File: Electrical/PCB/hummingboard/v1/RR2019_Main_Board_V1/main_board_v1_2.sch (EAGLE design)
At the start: 129 parts, among them CN1 MIRCO_B, J1 JTAG_SWD, J10 I2C_5V_4, J11 SERVO_LEFT, J12 SERVO_RIGHT, J13 ESC, J14 5V_INPUT, J15 QUAD_ENCODER_2, J17 I2C_5V_FXIO_1, J18 I2C_5V_FXIO_2, J2 REAR_ENCODER, J20 QUAD_ENCODER_1, J21 BLDC_HALL, J22 SPI_FXIO_1, J3 FRONT_ENCODER, J4 I2C_3V3_1, J5 SPI_2, J6 WIRELESS_MODULE, J7 UART_0, J8 UART_2, J9 STEERING_ANGLE, Q1 BSS138, Q2 BSS138, Q3 PMOS_SOT23, Q4 BSS138, Q5 BSS138, Q6 BSS138, Q7 BSS138, U1 MPU-9250(IMU)

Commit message: update on layout
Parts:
- added C23: TBD, RobotRacing2019_Master:CAP0603
- added J16: 7.2V_INPUT, RobotRacing2019_Master:PINHEAD-2-VERTICAL
- added L3: TBD, RobotRacing2019_Master:IND0603
- added R42: TBD, RobotRacing2019_Master:RES0603
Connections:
- removed net PTA11: U$50.1
- new net +7.2V: C23.1, J11.1, J12.1, L3.2
- new net N$34: J16.1, R42.2
- new net N$36: L3.1, R42.1
- net +5V: no longer J11.1, J12.1
- net GND: now also C23.2, J16.2
- net PTA11_/_FTM1_CH5: now also U$50.1
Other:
- moved on the sheet: J11, J12, J13

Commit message: [Journey Begins From Here] + new simulations and PCBs
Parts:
- removed J1: JTAG_SWD, RobotRacing2019_Master:10-PIN_SWD
- removed JP12: POWER_2, adafruit:PINHD-1X8BIG
- added C24: 0.1u, RobotRacing2019_Master:CAP0603
- added IC1: OR_SC70-5, RobotRacing2019_Master:OR_SC70-5
- added J19: JETSON_TRIGGER, RobotRacing2019_Master:PINHEAD-2-VERTICAL
- added Q8: BSS138, RobotRacing2019_Master:NMOS_SOT23
- added R43, R44: 10k, RobotRacing2019_Master:RES0603
- added U$44: TEAM_LOGO, RobotRacing2019_Master:TEAM_LOGO
- Q3: value PMOS_SOT23 -> DMP2066LSN
- U$12: value TEAM_LOGO -> SWD_1.27MM; device RobotRacing2019_Master:TEAM_LOGO -> RobotRacing2019_Master:SWD_1.27MM
- renumbered POWER_OFF/ON to OFF/ON
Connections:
- removed net 3V3: JP12.4, JP12.5, JP6.4, JP6.5
- removed net N$16: CN1.ID
- removed net VDD: C1.1, C2.1, C3.1, C4.1, C5.1, C6.1, J15.1, J17.1, J18.1, J20.1, J22.1, J5.1, JP12.1, JP12.2, JP12.3, JP6.1, JP6.2, JP6.3, R10.2, R11.2, R15.2, R18.2, R21.2, R22.2, R24.2, R26.2, R28.2, R29.2, R41.2, R9.2, U$1.VDD, U$1.VDD1, U$1.VDD2, U$1.VDD3, U$1.VDDA, U$1.VREFH
- new net N$35: J19.1, Q8.G
- new net N$38: IC1.A, Q8.D, R44.1
- new net N$39: IC1.OUT, Q3.G, R43.1
- net +3V3: now also JP6.4, JP6.5
- net +VDD: now also C1.1, C2.1, C24.2, C3.1, C4.1, C5.1, C6.1, IC1.VDD, J15.1, J17.1, J18.1, J20.1, J22.1, J5.1, JP6.1, JP6.2, JP6.3, R10.2, R11.2, R15.2, R18.2, R21.2, R22.2, R24.2, R26.2, R28.2, R29.2, R41.2, R43.2, R44.2, R9.2, U$1.VDD, U$1.VDD1, U$1.VDD2, U$1.VDD3, U$1.VDDA, U$1.VREFH, U$12.VCC; no longer J1.VCC
- net GND: now also C24.1, IC1.GND, Q8.S, U$12.GND, U$12.GND2, U$12.GND_DCT, U$12.KEY; no longer J1.GND, J1.GND2, J1.GND_DCT, J1.KEY, JP12.6, JP12.7, JP12.8
- net JTAG_TCLK/SWD_CLK: now also U$12.SWDCLK/TCK; no longer J1.SWDCLK/TCK
- net JTAG_TDI: now also U$12.NC/TDI; no longer J1.NC/TDI
- net JTAG_TDO/SWO: now also U$12.SWO/TDO; no longer J1.SWO/TDO
- net JTAG_TMS/SWD_DIO: now also U$12.SWDIO/TMS; no longer J1.SWDIO/TMS
- net JTAG_TRST_B: now also U$12./R/E/S/E/T; no longer J1./R/E/S/E/T
- net POWER_SHUT_DOWN: now also IC1.B; no longer Q3.G
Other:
- note added: "separe the 7.2V GND"
- note removed: "nominally LOW, turn high when overcurrent is measured - pick low Rds on - handle up to 300mA ?"
- moved on the sheet: C16, JP6

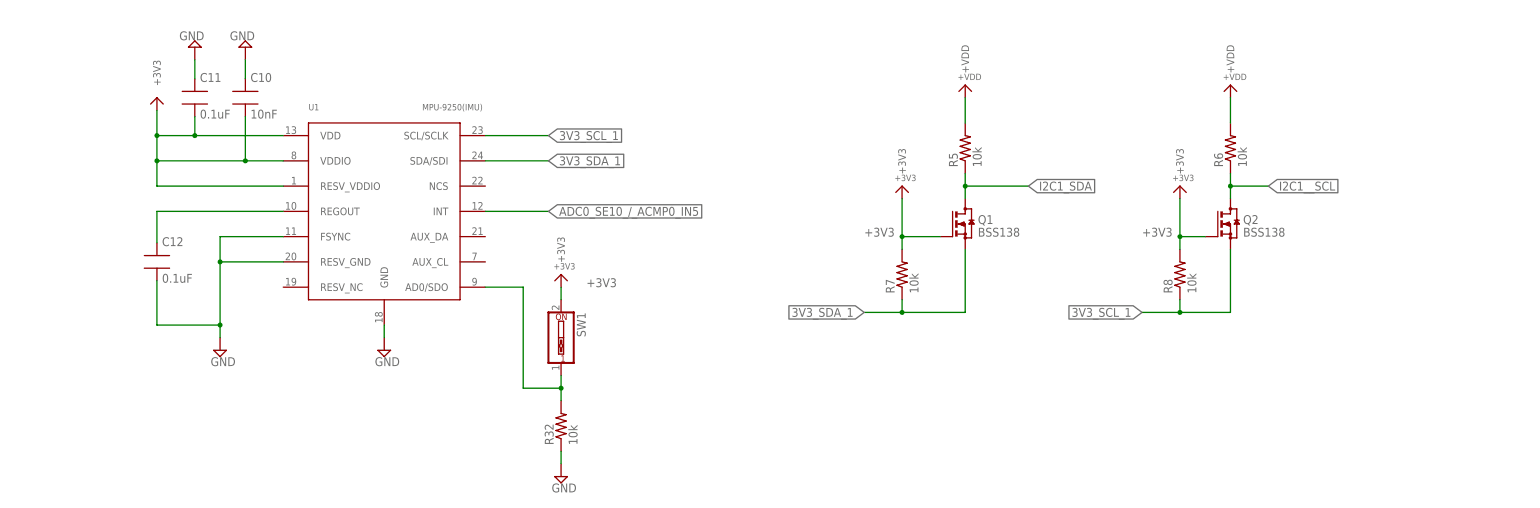
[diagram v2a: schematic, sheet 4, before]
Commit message: add 1.8V LDO and IMU change to ICM-20948
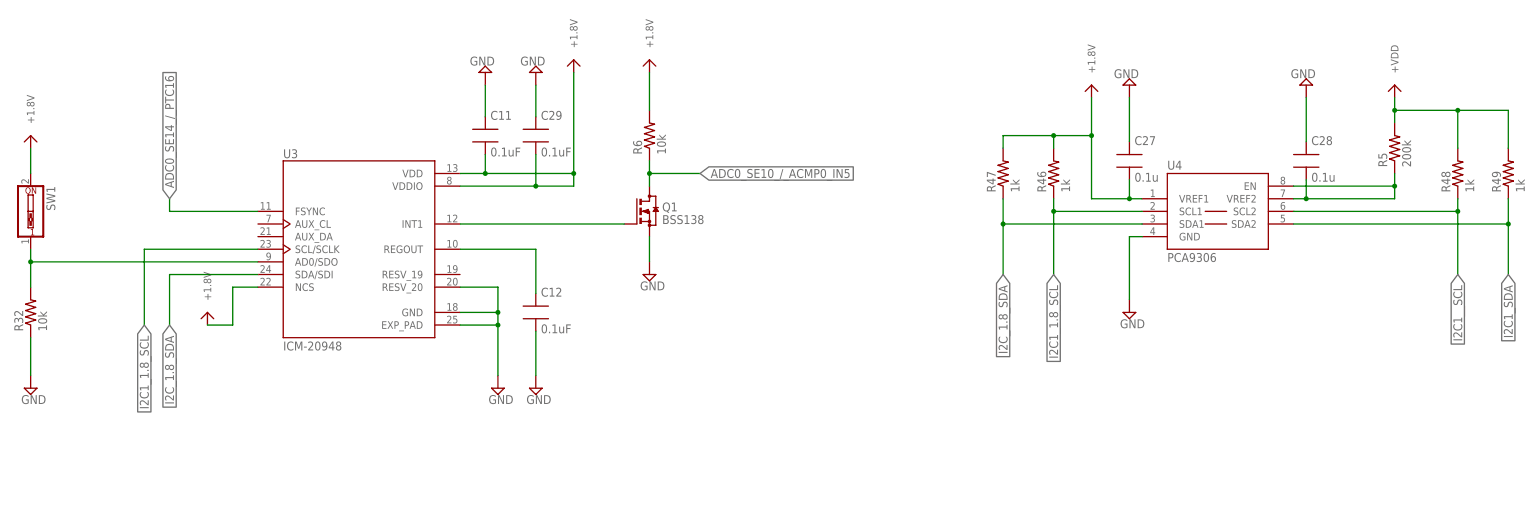
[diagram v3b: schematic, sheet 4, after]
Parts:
- removed C10: 10nF, RobotRacing2019_Master:CAP0603
- removed Q2: BSS138, RobotRacing2019_Master:NMOS_SOT23
- removed R7, R8: 10k, RobotRacing2019_Master:RES0603
- removed U1: MPU-9250(IMU), RobotRacing2019_Master:MPU-9250(IMU)
- added C25, C26: 1uF, RobotRacing2019_Master:CAP0603
- added C27, C28: 0.1u, RobotRacing2019_Master:CAP0603
- added C29: 0.1uF, RobotRacing2019_Master:CAP0603
- added D9: LED_GREEN, RobotRacing2019_Master:LED0603
- added R45: 150, RobotRacing2019_Master:RES0603
- added R46, R47, R48, R49: 1k, RobotRacing2019_Master:RES0603
- added U3: ICM-20948, RobotRacing2019_Master:ICM-20948
- added U4: PCA9306, RobotRacing2019_Master:PCA9306
- added VR2: ADP121-AUJZ18, RobotRacing2019_Master:ADP121
- D3, D4: value LED0603 -> LED_GREEN
- R3, R4: value (none) -> 150
- R5: value 10k -> 200k
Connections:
- new net +1.8V: C11.2, C26.1, C27.2, C29.2, R45.2, R46.2, R47.2, R6.2, SW1.2, U3.NCS, U3.VDD, U3.VDDIO, U4.VREF1, VR2.VOUT
- new net I2C1_1.8_SCL: R46.1, U3.SCL/SCLK, U4.SCL1
- new net I2C_1.8_SDA: R47.1, U3.SDA/SDI, U4.SDA1
- new net N$16: C28.2, R5.1, U4.EN, U4.VREF2
- new net N$37: Q1.G, U3.INT1
- new net N$42: D9.A, R45.1
- net +3V3: no longer C10.2, C11.2, Q1.G, Q2.G, R7.2, R8.2, SW1.2, U1.RESV_VDDIO, U1.VDD, U1.VDDIO
- net +VDD: now also C25.1, R48.2, R49.2, VR2.EN, VR2.VIN; no longer R6.2
- net 3V3_SCL_1: no longer Q2.S, R8.1, U1.SCL/SCLK
- net 3V3_SDA_1: no longer Q1.S, R7.1, U1.SDA/SDI
- net ADC0_SE10_/_ACMP0_IN5: now also Q1.D, R6.1; no longer U1.INT
- net ADC0_SE14_/_PTC16: now also U3.FSYNC
- net GND: now also C25.2, C26.2, C27.1, C28.1, C29.1, D9.C, Q1.S, U3.EXP_PAD, U3.GND, U3.RESV_20, U4.GND, VR2.GND; no longer C10.1, U1.FSYNC, U1.GND, U1.RESV_GND
- net I2C1_SDA: now also R49.1, U4.SDA2; no longer Q1.D, R5.1
- net I2C1__SCL: now also R48.1, U4.SCL2; no longer Q2.D, R6.1
- net N$10: now also U3.REGOUT; no longer U1.REGOUT
- net N$22: now also U3.AD0/SDO; no longer U1.AD0/SDO
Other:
- note added: "5V - 1.8 V LDO"
- note added: "IMU_FSYNC"
- note removed: "* can use AUX_DA / AUX_CL / FSYNC for external sensor via i2c"
- note removed: "pick mosfet with low RDS"
- moved on the sheet: C11, C12, Q1, R32, R5, R6, SW1

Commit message: signal connection complete
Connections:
- removed net 3V3_SCL_1: J4.3
- removed net 3V3_SDA_1: J4.4
- removed net I2C_1.8_SDA: R47.1, U3.SDA/SDI, U4.SDA1
- new net I2C1_1.8_SDA: J4.4, R47.1, U3.SDA/SDI, U4.SDA1
- net +1.8V: now also J4.1
- net +3V3: no longer J4.1
- net I2C1_1.8_SCL: now also J4.3
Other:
- note added: "5V-1V8 level shifter on page4"
- note added: "ICM-20948 in I2C config"
- note removed: "5V-3V3 level shifter on page4"
- note removed: "MPU9250 in I2C config"
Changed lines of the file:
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@@
 <part name="U$26" library="RobotRacing2019_Master" deviceset="+VDD" device=""/>
 <part name="U$28" library="RobotRacing2019_Master" deviceset="+VDD" device=""/>
-<part name="U$29" library="RobotRacing2019_Master" deviceset="+3V3" device=""/>
 <part name="U$30" library="RobotRacing2019_Master" deviceset="+VDD" device=""/>
 <part name="U$31" library="RobotRacing2019_Master" deviceset="+VDD" device=""/>
@@
 <part name="U$23" library="RobotRacing2019_Master" deviceset="+1V8" device=""/>
 <part name="U$24" library="RobotRacing2019_Master" deviceset="+1V8" device=""/>
+<part name="U$21" library="RobotRacing2019_Master" deviceset="+1V8" device=""/>
 </parts>
 <sheets>
@@
 <text x="-195.58" y="-15.24" size="1.778" layer="120">if AD0 -&gt; GND, i2c address = 1101000
 if AD0 -&gt; VDD, i2c address = 1101001</text>
-<text x="-99.06" y="20.32" size="2.54" layer="119">MPU9250 in I2C config</text>
-<text x="-132.08" y="-45.72" size="1.778" layer="117">TP / VIA</text>
-<text x="-119.38" y="-45.72" size="1.778" layer="117">TP / VIA</text>
+<text x="-99.06" y="20.32" size="2.54" layer="119">ICM-20948 in I2C config</text>
+<text x="-132.08" y="-53.34" size="1.778" layer="117">TP / VIA</text>
+<text x="-119.38" y="-53.34" size="1.778" layer="117">TP / VIA</text>
 </plain>
 <instances>
@@
 </segment>
 </net>
-<net name="I2C_1.8_SDA" class="0">
-<segment>
-<pinref part="U4" gate="G$1" pin="SDA1"/>
-<wire x1="76.2" y1="0" x2="48.26" y2="0" width="0.1524" layer="91"/>
-<pinref part="R47" gate="G$1" pin="1"/>
-<wire x1="48.26" y1="0" x2="48.26" y2="5.08" width="0.1524" layer="91"/>
-<wire x1="48.26" y1="0" x2="48.26" y2="-10.16" width="0.1524" layer="91"/>
-<junction x="48.26" y="0"/>
-<label x="48.26" y="-10.16" size="1.778" layer="95" rot="R270" xref="yes"/>
-</segment>
-<segment>
-<pinref part="U3" gate="G$1" pin="SDA/SDI"/>
-<wire x1="-101.6" y1="-10.16" x2="-119.38" y2="-10.16" width="0.1524" layer="91"/>
-<wire x1="-119.38" y1="-10.16" x2="-119.38" y2="-20.32" width="0.1524" layer="91"/>
-<label x="-119.38" y="-20.32" size="1.778" layer="95" rot="R270" xref="yes"/>
-</segment>
-</net>
 <net name="N$16" class="0">
 <segment>
@@
 </segment>
 </net>
+<net name="I2C1_1.8_SDA" class="0">
+<segment>
+<pinref part="U3" gate="G$1" pin="SDA/SDI"/>
+<wire x1="-101.6" y1="-10.16" x2="-119.38" y2="-10.16" width="0.1524" layer="91"/>
+<wire x1="-119.38" y1="-10.16" x2="-119.38" y2="-20.32" width="0.1524" layer="91"/>
+<label x="-119.38" y="-20.32" size="1.778" layer="95" rot="R270" xref="yes"/>
+</segment>
+<segment>
+<pinref part="U4" gate="G$1" pin="SDA1"/>
+<wire x1="76.2" y1="0" x2="48.26" y2="0" width="0.1524" layer="91"/>
+<pinref part="R47" gate="G$1" pin="1"/>
+<wire x1="48.26" y1="0" x2="48.26" y2="5.08" width="0.1524" layer="91"/>
+<wire x1="48.26" y1="0" x2="48.26" y2="-10.16" width="0.1524" layer="91"/>
+<junction x="48.26" y="0"/>
+<label x="48.26" y="-10.16" size="1.778" layer="95" rot="R270" xref="yes"/>
+</segment>
+</net>
 </nets>
 </sheet>
@@
 <wire x1="86.36" y1="-205.74" x2="12.7" y2="-205.74" width="0.1524" layer="206"/>
 <text x="-25.4" y="-101.6" size="1.778" layer="120">pull up on the MCU side</text>
-<text x="10.16" y="-101.6" size="1.778" layer="120">5V-3V3 level shifter on page4</text>
+<text x="10.16" y="-101.6" size="1.778" layer="120">5V-1V8 level shifter on page4</text>
 <text x="-20.32" y="91.44" size="1.778" layer="120">pull up and pull down on the MCU side</text>
 <text x="40.64" y="-261.62" size="1.778" layer="120">connect to uart of JETSON</text>
@@
 <attribute name="VALUE" x="-52.324" y="-100.584" size="1.27" layer="96"/>
 </instance>
-<instance part="U$29" gate="G$1" x="48.26" y="-106.68" smashed="yes">
-<attribute name="VALUE" x="44.196" y="-103.124" size="1.27" layer="96"/>
-</instance>
 <instance part="U$30" gate="G$1" x="-48.26" y="-236.22" smashed="yes">
 <attribute name="VALUE" x="-52.324" y="-235.204" size="1.27" layer="96"/>
@@
 <attribute name="VALUE" x="-12.7" y="116.84" size="1.27" layer="96"/>
 </instance>
+<instance part="U$21" gate="G$1" x="48.26" y="-106.68" smashed="yes"/>
 </instances>
 <busses>
@@
 </segment>
 </net>
-<net name="3V3_SCL_1" class="0">
+<net name="I2C1_1.8_SCL" class="0">
 <segment>
 <pinref part="J4" gate="G$1" pin="3"/>
@@
 </segment>
 </net>
-<net name="3V3_SDA_1" class="0">
+<net name="I2C1_1.8_SDA" class="0">
 <segment>
 <pinref part="J4" gate="G$1" pin="4"/>
@@
 <net name="+3V3" class="0">
 <segment>
-<pinref part="J4" gate="G$1" pin="1"/>
-<wire x1="30.48" y1="-111.76" x2="48.26" y2="-111.76" width="0.1524" layer="91"/>
-<wire x1="48.26" y1="-111.76" x2="73.66" y2="-111.76" width="0.1524" layer="91"/>
-<wire x1="48.26" y1="-111.76" x2="48.26" y2="-106.68" width="0.1524" layer="91"/>
-<junction x="48.26" y="-111.76"/>
-<pinref part="U$29" gate="G$1" pin="+3V3"/>
-<label x="38.1" y="-111.76" size="1.778" layer="95"/>
-</segment>
-<segment>
 <pinref part="J6" gate="G$1" pin="1"/>
 <wire x1="-33.02" y1="33.02" x2="-25.4" y2="33.02" width="0.1524" layer="91"/>
@@
 </segment>
 </net>
+<net name="+1.8V" class="0">
+<segment>
+<pinref part="J4" gate="G$1" pin="1"/>
+<wire x1="30.48" y1="-111.76" x2="48.26" y2="-111.76" width="0.1524" layer="91"/>
+<wire x1="48.26" y1="-111.76" x2="73.66" y2="-111.76" width="0.1524" layer="91"/>
+<wire x1="48.26" y1="-111.76" x2="48.26" y2="-106.68" width="0.1524" layer="91"/>
+<junction x="48.26" y="-111.76"/>
+<pinref part="U$21" gate="G$1" pin="+1.8V"/>
+</segment>
+</net>

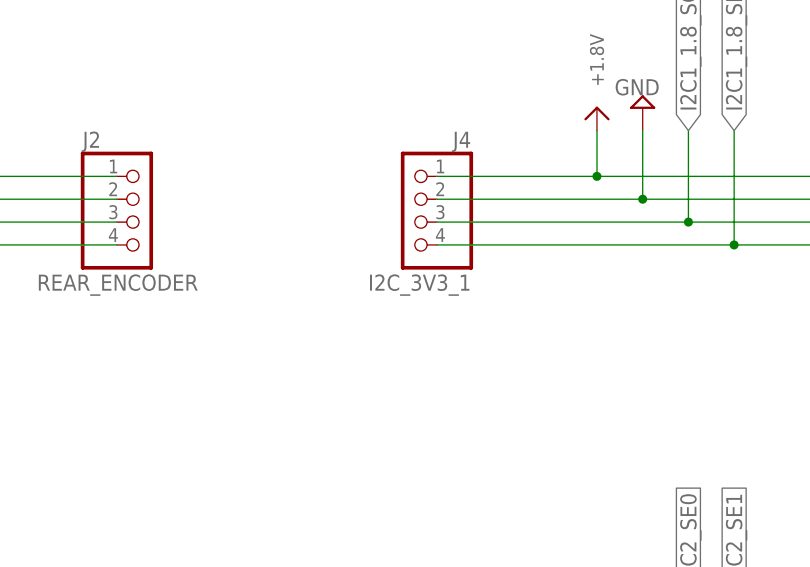
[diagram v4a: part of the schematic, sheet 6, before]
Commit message: add 1V8, 3V3, VUSB power plane
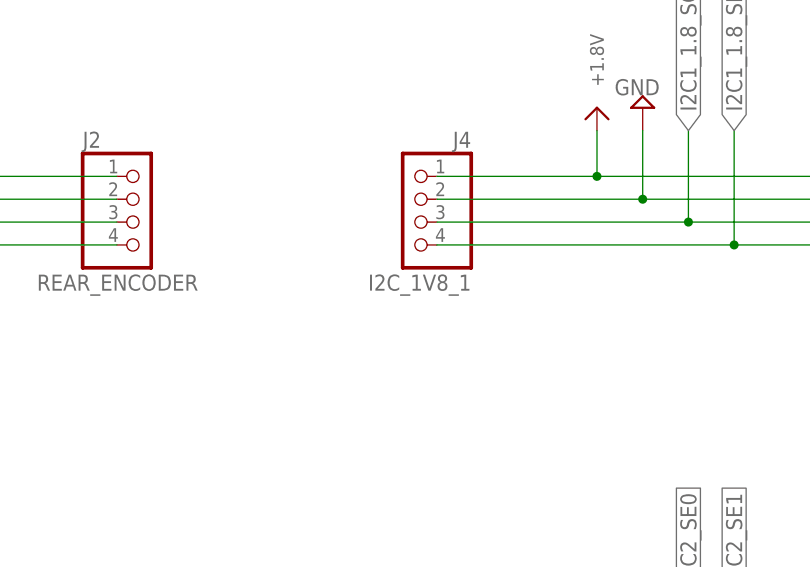
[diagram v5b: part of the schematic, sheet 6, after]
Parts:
- J4: value I2C_3V3_1 -> I2C_1V8_1
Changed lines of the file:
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@@
 <part name="J2" library="RobotRacing2019_Master" deviceset="PINHEAD-4-VERTICAL" device="" value="REAR_ENCODER"/>
 <part name="J3" library="RobotRacing2019_Master" deviceset="PINHEAD-4-VERTICAL" device="" value="FRONT_ENCODER"/>
-<part name="J4" library="RobotRacing2019_Master" deviceset="PINHEAD-4-VERTICAL" device="" value="I2C_3V3_1"/>
+<part name="J4" library="RobotRacing2019_Master" deviceset="PINHEAD-4-VERTICAL" device="" value="I2C_1V8_1"/>
 <part name="J5" library="RobotRacing2019_Master" deviceset="PINHEAD-6-VERTICAL" device="" value="SPI_2"/>
 <part name="J6" library="RobotRacing2019_Master" deviceset="PINHEAD-6-VERTICAL" device="" value="WIRELESS_MODULE"/>

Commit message: add silkscreen for pin info
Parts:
- JP6: value POWER_1 -> POWER
- renumbered U$50 to JP15
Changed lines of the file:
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@@
 <part name="SUPPLY56" library="RobotRacing2019_Master" deviceset="GND" device=""/>
 <part name="U$46" library="RobotRacing2019_Master" deviceset="+VDD" device=""/>
-<part name="JP6" library="adafruit" library_urn="urn:adsk.eagle:library:420" deviceset="PINHD-1X8" device="BIG" package3d_urn="urn:adsk.eagle:package:6240707/1" value="POWER_1"/>
+<part name="JP6" library="adafruit" library_urn="urn:adsk.eagle:library:420" deviceset="PINHD-1X8" device="BIG" package3d_urn="urn:adsk.eagle:package:6240707/1" value="POWER"/>
 <part name="U$47" library="RobotRacing2019_Master" deviceset="+3V3" device=""/>
 <part name="JP7" library="adafruit" library_urn="urn:adsk.eagle:library:420" deviceset="PINHD-1X3" device="" package3d_urn="urn:adsk.eagle:package:6240710/1" value="ADC_1"/>
 <part name="JP9" library="adafruit" library_urn="urn:adsk.eagle:library:420" deviceset="PINHD-1X8" device="BIG" package3d_urn="urn:adsk.eagle:package:6240707/1" value="ADC_2"/>
 <part name="JP14" library="adafruit" library_urn="urn:adsk.eagle:library:420" deviceset="PINHD-1X8" device="BIG" package3d_urn="urn:adsk.eagle:package:6240707/1" value="DIGITAL_1"/>
-<part name="U$50" library="adafruit" library_urn="urn:adsk.eagle:library:420" deviceset="PINHD-1X10" device="" package3d_urn="urn:adsk.eagle:package:6240656/1" value="DIGITAL_2"/>
+<part name="JP15" library="adafruit" library_urn="urn:adsk.eagle:library:420" deviceset="PINHD-1X10" device="" package3d_urn="urn:adsk.eagle:package:6240656/1" value="DIGITAL_2"/>
 <part name="SUPPLY58" library="RobotRacing2019_Master" deviceset="GND" device=""/>
 <part name="J21" library="RobotRacing2019_Master" deviceset="PINHEAD-6-VERTICAL" device="" value="BLDC_HALL"/>
@@
 <net name="N$39" class="0">
 <segment>
-<wire x1="-91.44" y1="-53.34" x2="-88.9" y2="-53.34" width="0.1524" layer="91"/>
 <pinref part="Q3" gate="G$1" pin="G"/>
 <wire x1="-88.9" y1="-53.34" x2="-86.36" y2="-53.34" width="0.1524" layer="91"/>
@@
 <pinref part="R43" gate="G$1" pin="1"/>
 <pinref part="IC1" gate="G$1" pin="OUT"/>
-<junction x="-88.9" y="-53.34"/>
 </segment>
 </net>
@@
 <attribute name="VALUE" x="39.37" y="-256.54" size="1.778" layer="96"/>
 </instance>
-<instance part="U$50" gate="G$1" x="45.72" y="-279.4" smashed="yes">
+<instance part="JP15" gate="G$1" x="45.72" y="-279.4" smashed="yes">
 <attribute name="NAME" x="39.37" y="-266.065" size="1.778" layer="95"/>
 <attribute name="VALUE" x="39.37" y="-297.18" size="1.778" layer="96"/>
@@
 </segment>
 <segment>
-<pinref part="U$50" gate="G$1" pin="10"/>
+<pinref part="JP15" gate="G$1" pin="10"/>
 <wire x1="43.18" y1="-292.1" x2="30.48" y2="-292.1" width="0.1524" layer="91"/>
 <pinref part="SUPPLY58" gate="GND" pin="GND"/>
@@
 <wire x1="43.18" y1="-271.78" x2="33.02" y2="-271.78" width="0.1524" layer="91"/>
 <label x="33.02" y="-271.78" size="1.778" layer="95" rot="R180" xref="yes"/>
-<pinref part="U$50" gate="G$1" pin="2"/>
+<pinref part="JP15" gate="G$1" pin="2"/>
 </segment>
 </net>
@@
 <wire x1="43.18" y1="-274.32" x2="-20.32" y2="-274.32" width="0.1524" layer="91"/>
 <label x="-20.32" y="-274.32" size="1.778" layer="95" rot="R180" xref="yes"/>
-<pinref part="U$50" gate="G$1" pin="3"/>
+<pinref part="JP15" gate="G$1" pin="3"/>
 </segment>
 </net>
@@
 <wire x1="43.18" y1="-276.86" x2="33.02" y2="-276.86" width="0.1524" layer="91"/>
 <label x="33.02" y="-276.86" size="1.778" layer="95" rot="R180" xref="yes"/>
-<pinref part="U$50" gate="G$1" pin="4"/>
+<pinref part="JP15" gate="G$1" pin="4"/>
 </segment>
 </net>
@@
 <wire x1="43.18" y1="-279.4" x2="-20.32" y2="-279.4" width="0.1524" layer="91"/>
 <label x="-20.32" y="-279.4" size="1.778" layer="95" rot="R180" xref="yes"/>
-<pinref part="U$50" gate="G$1" pin="5"/>
+<pinref part="JP15" gate="G$1" pin="5"/>
 </segment>
 </net>
@@
 <wire x1="43.18" y1="-281.94" x2="33.02" y2="-281.94" width="0.1524" layer="91"/>
 <label x="33.02" y="-281.94" size="1.778" layer="95" rot="R180" xref="yes"/>
-<pinref part="U$50" gate="G$1" pin="6"/>
+<pinref part="JP15" gate="G$1" pin="6"/>
 </segment>
 </net>
@@
 <wire x1="43.18" y1="-284.48" x2="-20.32" y2="-284.48" width="0.1524" layer="91"/>
 <label x="-20.32" y="-284.48" size="1.778" layer="95" rot="R180" xref="yes"/>
-<pinref part="U$50" gate="G$1" pin="7"/>
+<pinref part="JP15" gate="G$1" pin="7"/>
 </segment>
 </net>
@@
 <wire x1="33.02" y1="-287.02" x2="43.18" y2="-287.02" width="0.1524" layer="91"/>
 <label x="33.02" y="-287.02" size="1.778" layer="95" rot="R180" xref="yes"/>
-<pinref part="U$50" gate="G$1" pin="8"/>
+<pinref part="JP15" gate="G$1" pin="8"/>
 </segment>
 </net>
@@
 <wire x1="43.18" y1="-289.56" x2="-20.32" y2="-289.56" width="0.1524" layer="91"/>
 <label x="-20.32" y="-289.56" size="1.778" layer="95" rot="R180" xref="yes"/>
-<pinref part="U$50" gate="G$1" pin="9"/>
+<pinref part="JP15" gate="G$1" pin="9"/>
 </segment>
 </net>
 <net name="PTA11_/_FTM1_CH5" class="0">
 <segment>
-<pinref part="U$50" gate="G$1" pin="1"/>
+<pinref part="JP15" gate="G$1" pin="1"/>
 <wire x1="43.18" y1="-269.24" x2="-20.32" y2="-269.24" width="0.1524" layer="91"/>
 <label x="-20.32" y="-269.24" size="1.778" layer="95" rot="R180" xref="yes"/>
